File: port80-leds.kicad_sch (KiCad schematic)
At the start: 36 parts, among them U6001 SN74AC7541_VQFN, U6009 SN74AC7541_VQFN

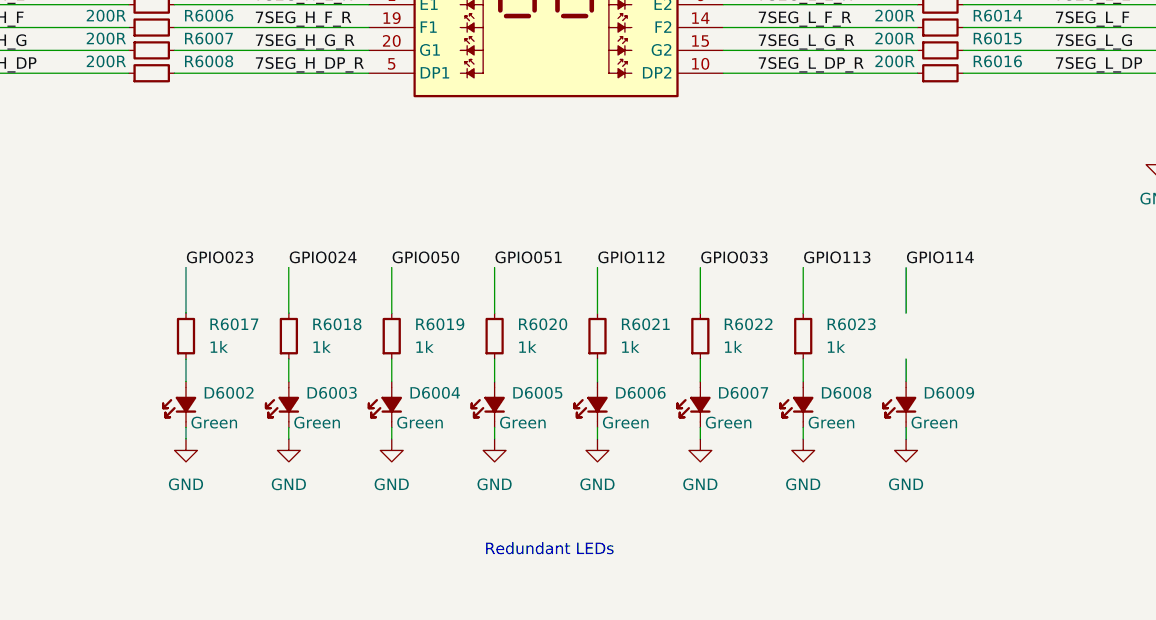
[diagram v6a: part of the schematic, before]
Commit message: [#103696] Change redundant LED connections, place LEDs on PCB
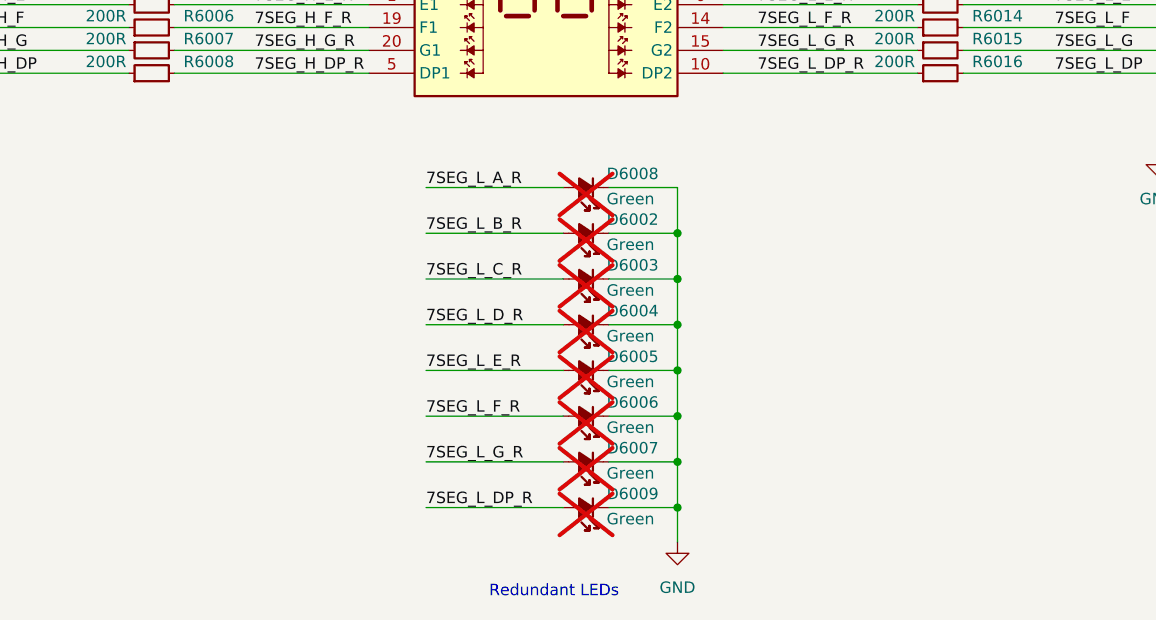
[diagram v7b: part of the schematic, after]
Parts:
- removed R6017, R6018, R6019, R6020, R6021, R6022, R6023: R_1k_0402, antmicro-footprints:R_0402_1005Metric, symbol Antmicro Symbols:R_1k_0402
- D6002, D6003, D6004, D6005, D6006, D6007, D6008, D6009: now not fitted
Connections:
- net 7SEG_L_A_R: now also D6008.2 (A)
- net 7SEG_L_B_R: now also D6002.2 (A)
- net 7SEG_L_C_R: now also D6003.2 (A)
- net 7SEG_L_DP_R: now also D6009.2 (A)
- net 7SEG_L_D_R: now also D6004.2 (A)
- net 7SEG_L_E_R: now also D6005.2 (A)
- net 7SEG_L_F_R: now also D6006.2 (A)
- net 7SEG_L_G_R: now also D6007.2 (A)

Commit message: [#103753] Update symbol libraries
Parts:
- C6001, C6002: symbol Capacitors0402:C_100n_0402 -> antmicroCapacitors0402:C_100n_0402
- D6001: symbol Antmicro Symbols:ACDA02-41SURKWA-F01 -> antmicroLEDIndicationDiscrete:ACDA02-41SURKWA-F01
- R6001, R6002, R6003, R6004, R6005, R6006, R6007, R6008, R6009, R6010, R6011, R6012, R6013, R6014, R6015, R6016: symbol Antmicro Symbols:R_200R_0402 -> antmicroResistors0402:R_200R_0402
- U6001, U6009: symbol Antmicro Symbols:SN74AC7541_VQFN -> antmicroLogicBuffersDriversReceiversTransceivers:SN74AC7541_VQFN
